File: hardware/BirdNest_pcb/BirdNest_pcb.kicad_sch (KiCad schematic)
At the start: 33 parts, among them J1 Solarpanel, J2 AM312 connector, Q1 FQP27P06, Q5 FQP27P06, U1 DS18B20, U4 ESP32-CAM, U5 TP4056_Module, U6 VXO7803-500

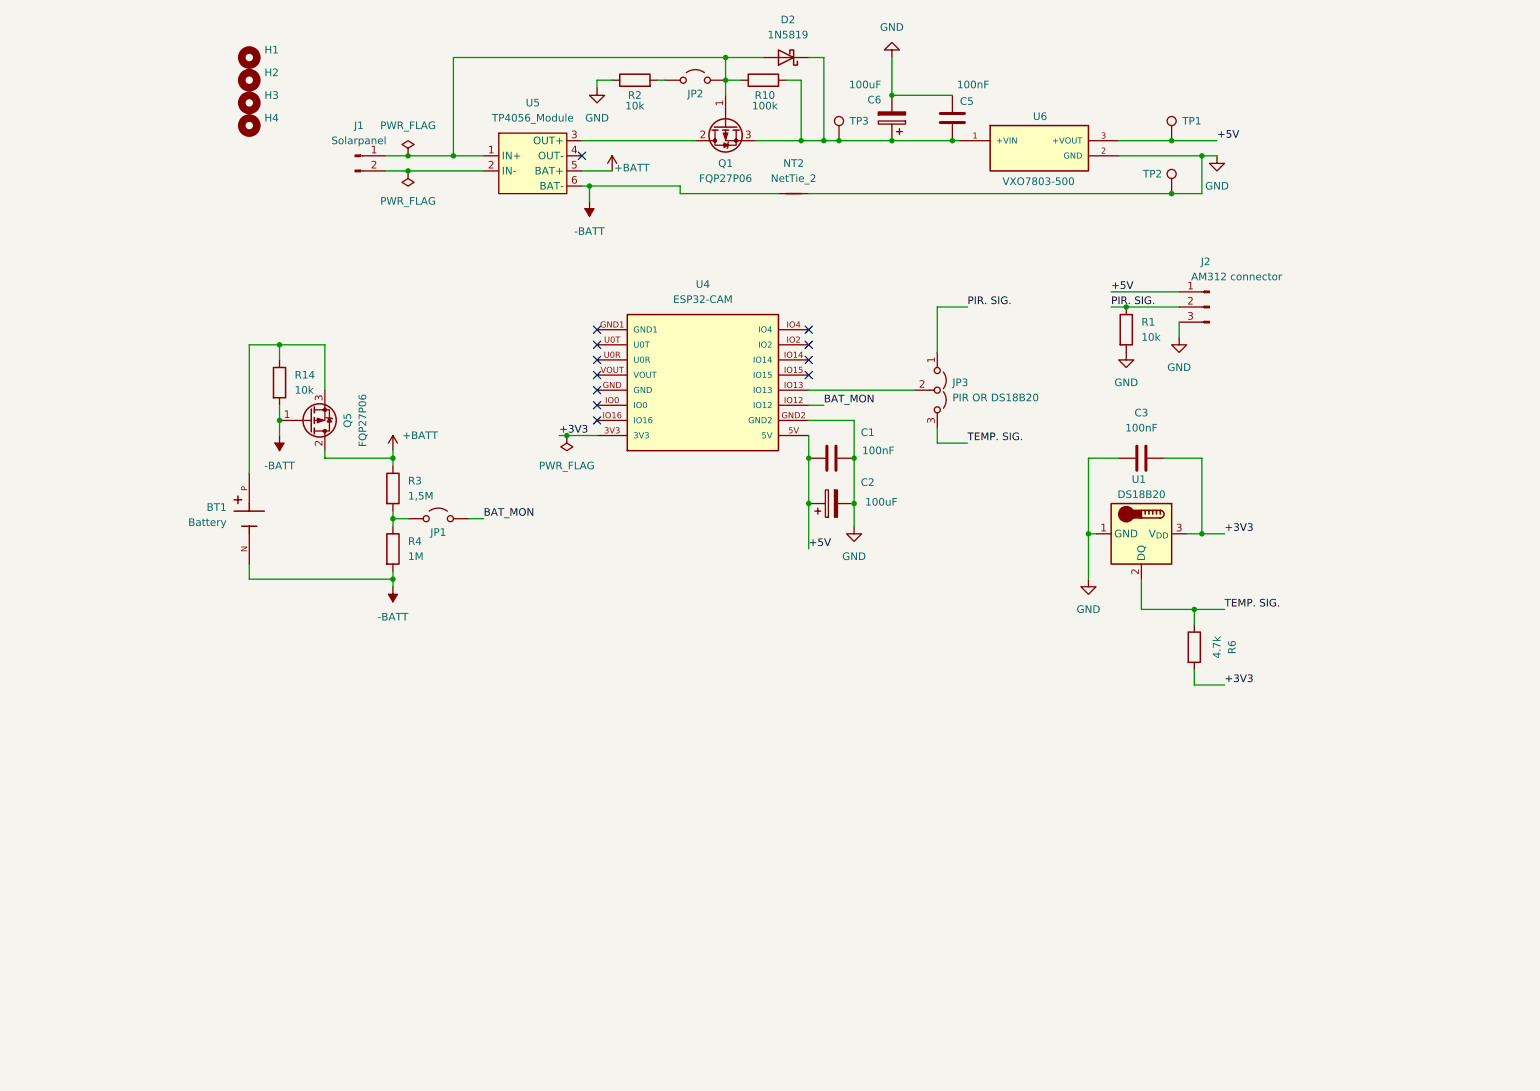
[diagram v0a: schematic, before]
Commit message: feat: single-binary multi-device model + GitHub OTA (v0.1.0)
- Runtime device identity (label/hostname) via NVS, MAC-based fallback
- OTA-compatible partition table (A/B, 2x1.9MB) replacing min_spiffs
- FW versioning via git tag (scripts/fw_version_from_git.py)
- GitHub OTA module: check/install/rollback with SHA-256 verification
- MQTT OTA event telemetry (mqttPublishOtaEvent)
- New Telegram commands: /otastatus /otaupdate_check /otaupdate_now
  /otaupdate_auto_on|off /otachannel /otatoken_set /otatoken_clear
  /setlabel /sethostname /bootstrap_prepare /reboot_ota
- CI release workflow: 1 bin + 1 manifest per git tag
- Bootstrap preflight for safe first remote install
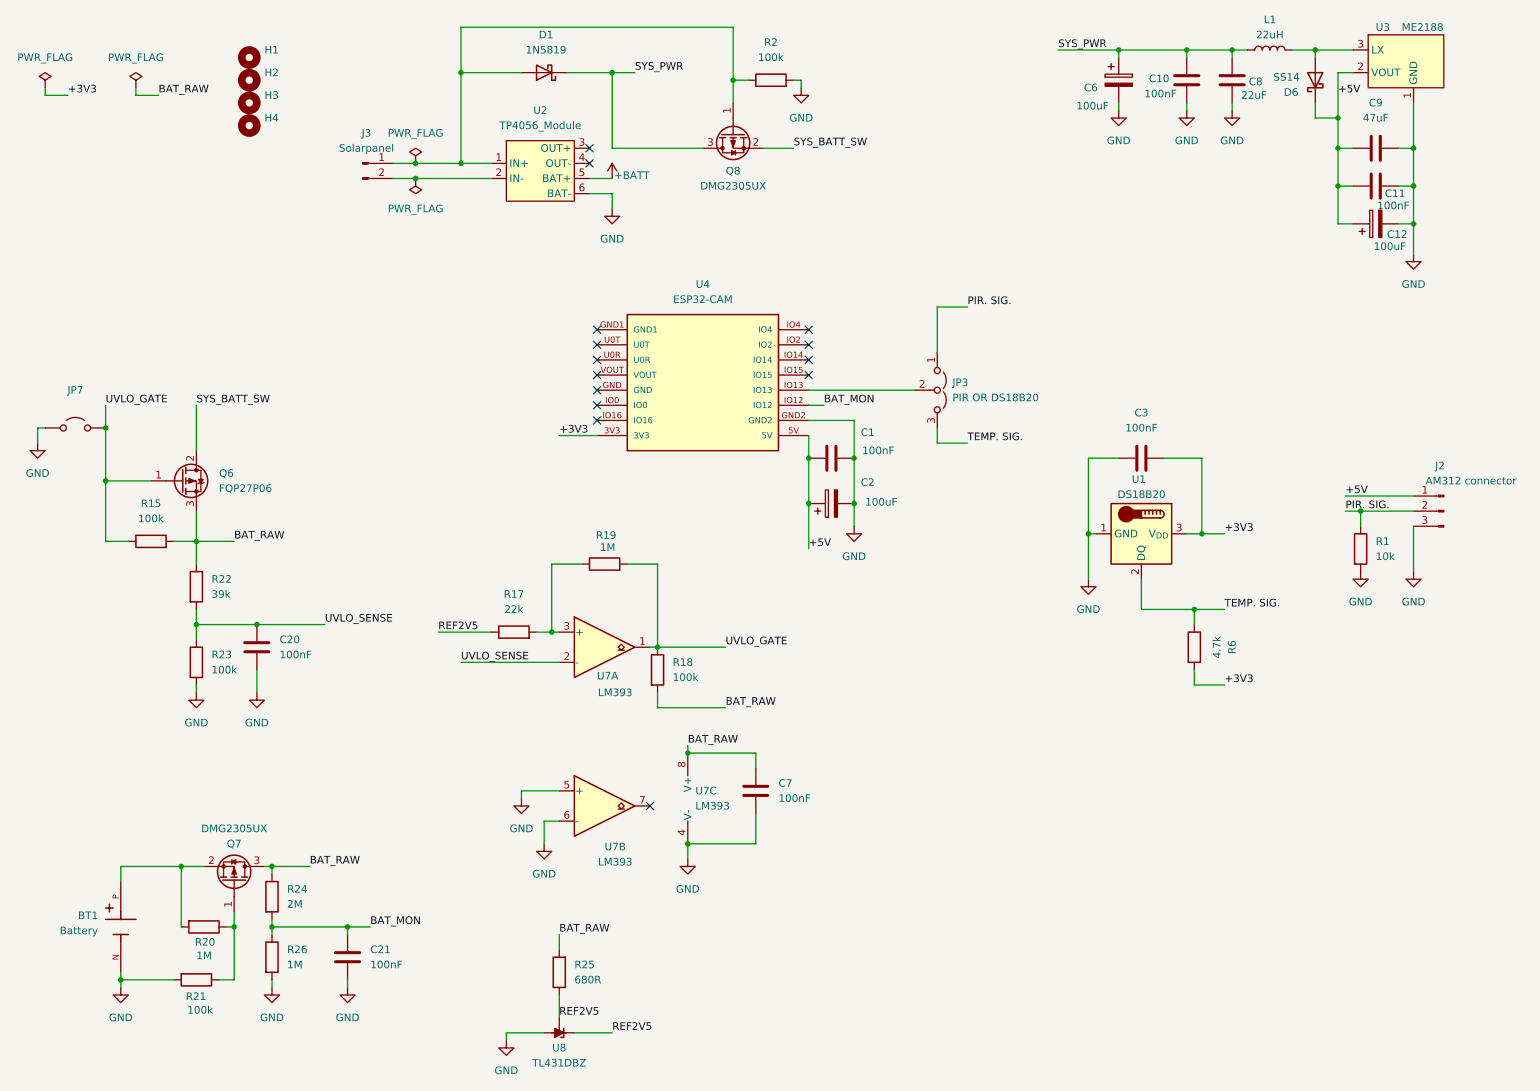
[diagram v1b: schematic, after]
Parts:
- removed C5: 100nF, Capacitor_THT:C_Disc_D5.0mm_W2.5mm_P2.50mm, symbol Device:C
- removed D2: 1N5819, Diode_THT:D_DO-41_SOD81_P10.16mm_Horizontal, symbol Diode:1N5819
- removed J1: Solarpanel, Connector_PinHeader_2.54mm:PinHeader_1x02_P2.54mm_Vertical, symbol Connector:Conn_01x02_Pin
- removed JP1, JP2: Jumper_2_Open, Connector_PinHeader_2.54mm:PinHeader_1x02_P2.54mm_Vertical, symbol Jumper:Jumper_2_Open
- removed NT2: NetTie_2, NetTie:NetTie-2_THT_Pad1.0mm, symbol Device:NetTie_2
- removed Q1, Q5: FQP27P06, Package_TO_SOT_THT:TO-220-3_Vertical, symbol Transistor_FET:FQP27P06
- removed R10: 100k, Resistor_THT:R_Axial_DIN0207_L6.3mm_D2.5mm_P10.16mm_Horizontal, symbol Device:R
- removed R14: 10k, Resistor_THT:R_Axial_DIN0207_L6.3mm_D2.5mm_P10.16mm_Horizontal, symbol Device:R
- removed R3: 1,5M, Resistor_THT:R_Axial_DIN0207_L6.3mm_D2.5mm_P10.16mm_Horizontal, symbol Device:R
- removed R4: 1M, Resistor_THT:R_Axial_DIN0207_L6.3mm_D2.5mm_P10.16mm_Horizontal, symbol Device:R
- removed TP1, TP2, TP3: TestPoint, TestPoint:TestPoint_Pad_1.5x1.5mm, symbol Connector:TestPoint
- removed U5: TP4056_Module, MyFootprints:TP4056-Module, symbol TP4056:TP4056
- removed U6: VXO7803-500, VXO7803-500:CONV_VXO7803-500, symbol VXO7803-500:VXO7803-500
- added C10, C11, C20, C21, C7: 100nF, Capacitor_SMD:C_1206_3216Metric_Pad1.33x1.80mm_HandSolder, symbol Device:C
- added C12: 100uF, Capacitor_THT:CP_Radial_D6.3mm_P2.50mm, symbol Device:C_Polarized
- added C8: 22uF, Capacitor_SMD:C_1206_3216Metric_Pad1.33x1.80mm_HandSolder, symbol Device:C
- added C9: 47uF, Capacitor_SMD:C_1206_3216Metric_Pad1.33x1.80mm_HandSolder, symbol Device:C
- added D1: 1N5819, Diode_THT:D_DO-41_SOD81_P10.16mm_Horizontal, symbol Diode:1N5819
- added D6: SS14, Diode_SMD:D_SMA-SMB_Universal_Handsoldering, symbol Device:D_Schottky
- added J3: Solarpanel, Connector_PinHeader_2.54mm:PinHeader_1x02_P2.54mm_Vertical, symbol Connector:Conn_01x02_Pin
- added JP7: Jumper_2_Open, Connector_PinHeader_2.54mm:PinHeader_1x02_P2.54mm_Vertical, symbol Jumper:Jumper_2_Open
- added L1: 22uH, Inductor_SMD:L_10.4x10.4_H4.8, symbol Device:L
- added Q6: FQP27P06, Package_TO_SOT_THT:TO-220-3_Vertical, symbol Transistor_FET:FQP27P06
- added Q7, Q8: DMG2305UX, DMG2305UX:SOT23, symbol Transistor_FET:Q_PMOS_GSD
- added R15, R18, R21, R23: 100k, Resistor_THT:R_Axial_DIN0207_L6.3mm_D2.5mm_P10.16mm_Horizontal, symbol Device:R
- added R17: 22k, Resistor_THT:R_Axial_DIN0207_L6.3mm_D2.5mm_P10.16mm_Horizontal, symbol Device:R
- added R19, R20, R26: 1M, Resistor_THT:R_Axial_DIN0207_L6.3mm_D2.5mm_P10.16mm_Horizontal, symbol Device:R
- added R22: 39k, Resistor_THT:R_Axial_DIN0207_L6.3mm_D2.5mm_P10.16mm_Horizontal, symbol Device:R
- added R24: 2M, Resistor_THT:R_Axial_DIN0207_L6.3mm_D2.5mm_P10.16mm_Horizontal, symbol Device:R
- added R25: 680R, Resistor_THT:R_Axial_DIN0207_L6.3mm_D2.5mm_P10.16mm_Horizontal, symbol Device:R
- added U2: TP4056_Module, MyFootprints:TP4056-Module, symbol TP4056:TP4056
- added U3: ME2188, Package_TO_SOT_SMD:SOT-89-3, symbol my_symbols:ME2188A50
- added U7: LM393, Package_DIP:DIP-8_W7.62mm, symbol Comparator:LM393
- added U8: TL431DBZ, Package_TO_SOT_SMD:SOT-23, symbol Reference_Voltage:TL431DBZ
- R2: value 10k -> 100k
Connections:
- net -BATT is gone; now on net GND: BT1.N
- net +5V: now also C11.2, C12.1, C9.1, D6.1 (K), U3.2 (VOUT)
- net +BATT: now also U2.5 (BAT+)
- net BAT_MON: now also C21.1, R24.2, R26.1
- net GND: now also R2.2, C10.2, C11.1, C12.2, C20.2, C21.2, C7.2, C8.2, C9.2, JP7.1 (A), R21.2, R23.2, R26.2, U2.6 (BAT-), U3.1 (GND), U7.4 (V-), U7.5 (+), U7.6 (-), U8.3 (A); no longer R2.1
- net SYS_PWR: now reaches C6.1
- net SYS_PWR: now also C10.1, C8.1, D1.1 (K), L1.1, Q8.3 (D)
- net at BT1.P: now also Q7.2 (S), R20.2
- new net: D6.2 (A), L1.2, U3.3 (LX)
- new net: D1.2 (A), J3.1 (Pin_1), Q8.1 (G), R2.1, U2.1 (IN+)
- new net: R17.2, R19.1, U7.3 (+)
- new net: Q7.1 (G), R20.1, R21.1
- new net: J3.2 (Pin_2), U2.2 (IN-)
- new net BAT_RAW: C7.1, Q6.3 (S), Q7.3 (D), R15.2, R18.2, R22.1, R24.1, R25.2, U7.8 (V+)
- new net REF2V5: R17.1, R25.1, U8.1 (K), U8.2 (REF)
- new net SYS_BATT_SW: Q6.2 (D), Q8.2 (S)
- new net UVLO_GATE: JP7.2 (B), Q6.1 (G), R15.1, R18.1, R19.2, U7.1
- new net UVLO_SENSE: C20.1, R22.2, R23.1, U7.2 (-)
- no-connect marks 12 -> 14
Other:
- moved on the sheet: J2, R1

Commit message: hw: update BirdNest PCB design files
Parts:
- C1, C3: footprint Capacitor_THT:C_Disc_D5.0mm_W2.5mm_P2.50mm -> Capacitor_SMD:C_1206_3216Metric_Pad1.33x1.80mm_HandSolder
- J2: footprint Connector_PinHeader_2.54mm:PinHeader_1x03_P2.54mm_Vertical -> TerminalBlock_Phoenix:TerminalBlock_Phoenix_MKDS-1,5-3-5.08_1x03_P5.08mm_Horizontal
- J3: footprint Connector_PinHeader_2.54mm:PinHeader_1x02_P2.54mm_Vertical -> TerminalBlock_Phoenix:TerminalBlock_Phoenix_MKDS-1,5-2-5.08_1x02_P5.08mm_Horizontal
- R1, R15, R17, R18, R19, R2, R20, R21, R22, R23, R24, R25, R26, R6: footprint Resistor_THT:R_Axial_DIN0207_L6.3mm_D2.5mm_P10.16mm_Horizontal -> Resistor_SMD:R_1206_3216Metric_Pad1.30x1.75mm_HandSolder
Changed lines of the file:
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@@
 			)
 		)
-		(property "Footprint" "Resistor_THT:R_Axial_DIN0207_L6.3mm_D2.5mm_P10.16mm_Horizontal"
+		(property "Footprint" "Resistor_SMD:R_1206_3216Metric_Pad1.30x1.75mm_HandSolder"
 			(at 212.852 121.92 90)
 			(hide yes)
@@
 			)
 		)
-		(property "Footprint" "Resistor_THT:R_Axial_DIN0207_L6.3mm_D2.5mm_P10.16mm_Horizontal"
+		(property "Footprint" "Resistor_SMD:R_1206_3216Metric_Pad1.30x1.75mm_HandSolder"
 			(at 57.912 163.83 90)
 			(hide yes)
@@
 			)
 		)
-		(property "Footprint" "Resistor_THT:R_Axial_DIN0207_L6.3mm_D2.5mm_P10.16mm_Horizontal"
+		(property "Footprint" "Resistor_SMD:R_1206_3216Metric_Pad1.30x1.75mm_HandSolder"
 			(at 240.792 105.41 90)
 			(hide yes)
@@
 			)
 		)
-		(property "Footprint" "Resistor_THT:R_Axial_DIN0207_L6.3mm_D2.5mm_P10.16mm_Horizontal"
+		(property "Footprint" "Resistor_SMD:R_1206_3216Metric_Pad1.30x1.75mm_HandSolder"
 			(at 143.51 28.448 90)
 			(hide yes)
@@
 			)
 		)
-		(property "Footprint" "Connector_PinHeader_2.54mm:PinHeader_1x03_P2.54mm_Vertical"
+		(property "Footprint" "TerminalBlock_Phoenix:TerminalBlock_Phoenix_MKDS-1,5-3-5.08_1x03_P5.08mm_Horizontal"
 			(at 256.54 99.06 0)
 			(hide yes)
@@
 			)
 		)
-		(property "Footprint" "Resistor_THT:R_Axial_DIN0207_L6.3mm_D2.5mm_P10.16mm_Horizontal"
+		(property "Footprint" "Resistor_SMD:R_1206_3216Metric_Pad1.30x1.75mm_HandSolder"
 			(at 115.57 109.728 90)
 			(hide yes)
@@
 			)
 		)
-		(property "Footprint" "Resistor_THT:R_Axial_DIN0207_L6.3mm_D2.5mm_P10.16mm_Horizontal"
+		(property "Footprint" "Resistor_SMD:R_1206_3216Metric_Pad1.30x1.75mm_HandSolder"
 			(at 46.99 176.022 90)
 			(hide yes)
@@
 			)
 		)
-		(property "Footprint" "Resistor_THT:R_Axial_DIN0207_L6.3mm_D2.5mm_P10.16mm_Horizontal"
+		(property "Footprint" "Resistor_SMD:R_1206_3216Metric_Pad1.30x1.75mm_HandSolder"
 			(at 45.212 124.46 90)
 			(hide yes)
@@
 			)
 		)
-		(property "Footprint" "Resistor_THT:R_Axial_DIN0207_L6.3mm_D2.5mm_P10.16mm_Horizontal"
+		(property "Footprint" "Resistor_SMD:R_1206_3216Metric_Pad1.30x1.75mm_HandSolder"
 			(at 48.26 167.132 90)
 			(hide yes)
@@
 			)
 		)
-		(property "Footprint" "Resistor_THT:R_Axial_DIN0207_L6.3mm_D2.5mm_P10.16mm_Horizontal"
+		(property "Footprint" "Resistor_SMD:R_1206_3216Metric_Pad1.30x1.75mm_HandSolder"
 			(at 39.37 105.918 90)
 			(hide yes)
@@
 			)
 		)
-		(property "Footprint" "Resistor_THT:R_Axial_DIN0207_L6.3mm_D2.5mm_P10.16mm_Horizontal"
+		(property "Footprint" "Resistor_SMD:R_1206_3216Metric_Pad1.30x1.75mm_HandSolder"
 			(at 100.33 121.158 90)
 			(hide yes)
@@
 			)
 		)
-		(property "Footprint" "Resistor_THT:R_Axial_DIN0207_L6.3mm_D2.5mm_P10.16mm_Horizontal"
+		(property "Footprint" "Resistor_SMD:R_1206_3216Metric_Pad1.30x1.75mm_HandSolder"
 			(at 122.682 125.73 90)
 			(hide yes)
@@
 			)
 		)
-		(property "Footprint" "Capacitor_THT:C_Disc_D5.0mm_W2.5mm_P2.50mm"
+		(property "Footprint" "Capacitor_SMD:C_1206_3216Metric_Pad1.33x1.80mm_HandSolder"
 			(at 157.48 89.2048 0)
 			(hide yes)
@@
 			)
 		)
-		(property "Footprint" "Resistor_THT:R_Axial_DIN0207_L6.3mm_D2.5mm_P10.16mm_Horizontal"
+		(property "Footprint" "Resistor_SMD:R_1206_3216Metric_Pad1.30x1.75mm_HandSolder"
 			(at 109.728 176.53 90)
 			(hide yes)
@@
 			)
 		)
-		(property "Footprint" "Connector_PinHeader_2.54mm:PinHeader_1x02_P2.54mm_Vertical"
+		(property "Footprint" "TerminalBlock_Phoenix:TerminalBlock_Phoenix_MKDS-1,5-2-5.08_1x02_P5.08mm_Horizontal"
 			(at 74.93 40.64 0)
 			(hide yes)
@@
 			)
 		)
-		(property "Footprint" "Capacitor_THT:C_Disc_D5.0mm_W2.5mm_P2.50mm"
+		(property "Footprint" "Capacitor_SMD:C_1206_3216Metric_Pad1.33x1.80mm_HandSolder"
 			(at 209.55 89.2048 0)
 			(hide yes)
@@
 			)
 		)
-		(property "Footprint" "Resistor_THT:R_Axial_DIN0207_L6.3mm_D2.5mm_P10.16mm_Horizontal"
+		(property "Footprint" "Resistor_SMD:R_1206_3216Metric_Pad1.30x1.75mm_HandSolder"
 			(at 57.912 173.99 90)
 			(hide yes)
@@
 			)
 		)
-		(property "Footprint" "Resistor_THT:R_Axial_DIN0207_L6.3mm_D2.5mm_P10.16mm_Horizontal"
+		(property "Footprint" "Resistor_SMD:R_1206_3216Metric_Pad1.30x1.75mm_HandSolder"
 			(at 45.212 111.76 90)
 			(hide yes)
